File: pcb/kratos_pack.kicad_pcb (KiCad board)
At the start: 4 copper layers, 44.2 x 20.2 mm, 121 parts, among them J1 USB_C_Receptacle_USB2.0, J2 PROG_CONN, J3 DBG_UART, J4 BAT_MID+NTC, J5 BAT_7.4V, J6 BAT_0V, J7 OUT+, J8 OUT-, Q1 AON7403, Q2 AON7414, Q3 AON7414, Q4 UT6MA2TCR, Q5 UT6MA2TCR, Q6 UT6MA2TCR, SW1 WAKEUP, SW2 BOOT, SW3 RST_BTN, U1 USBLC6-2SC6, U10 24LC32, U11 MIC94300, U12 74LVC2G14, U13 MIC94300, U2 CP2102N-Axx-xQFN20, U3 STM32G071Gx, U4 KTD2026BEWE, U5 BQ25887, U6 BD48xxFVE, U7 INA199, U8 LTC4231, U9 LDK715M33R

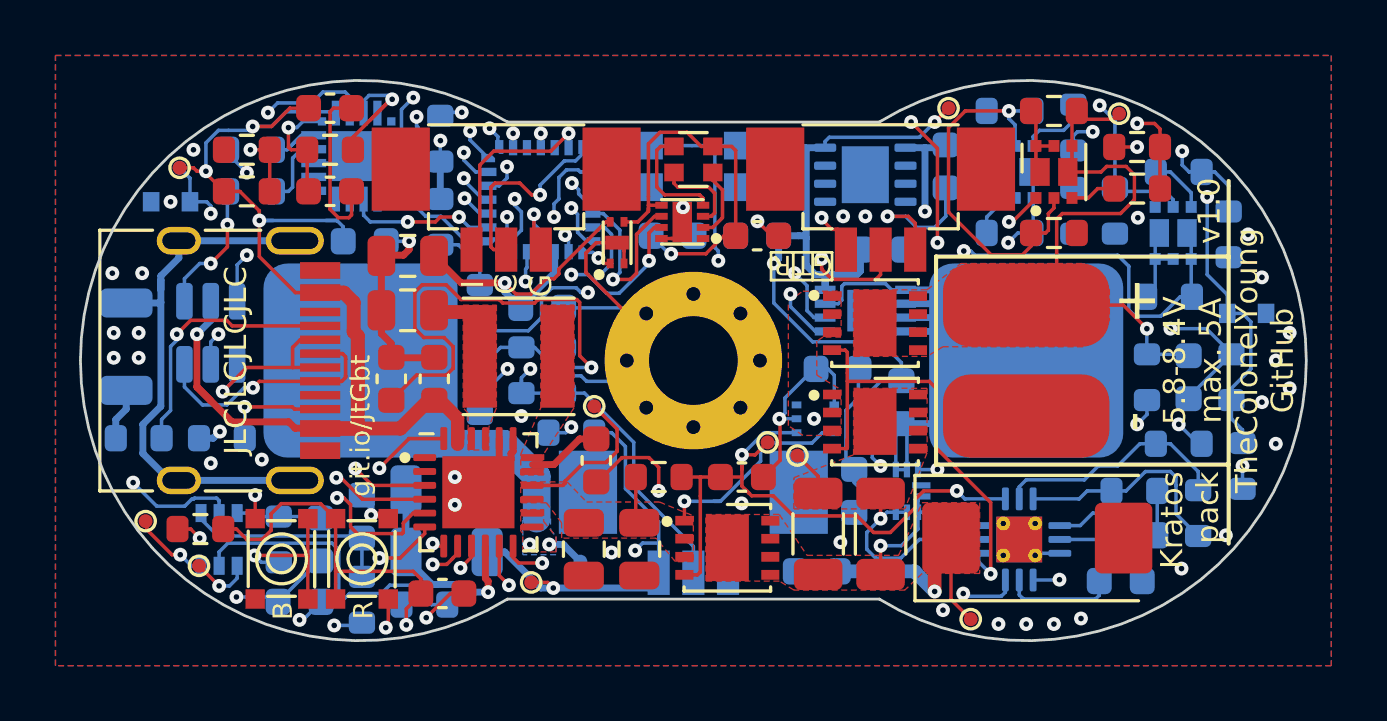
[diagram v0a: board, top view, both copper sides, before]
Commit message: Schema & PCB: add pull up to wakeup button
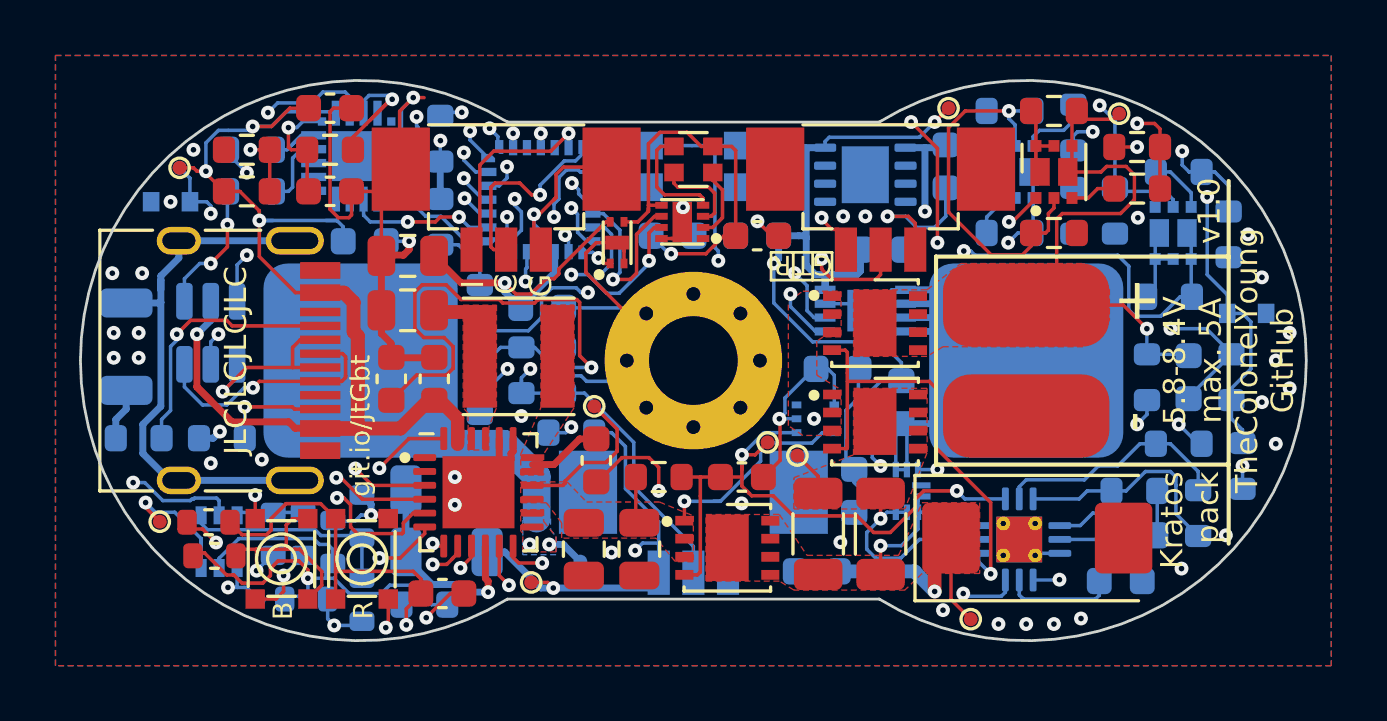
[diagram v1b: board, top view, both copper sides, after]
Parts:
- added R43: R, TCY_passives:R_0603_1608Metric, B.Cu at (137.0, 108.6)
- added R44: R, TCY_passives:R_0603_1608Metric, F.Cu at (133.7, 107.0)
- C1, C27, C28: footprint Capacitor_SMD:C_0603_1608Metric -> TCY_passives:C_0603_1608Metric
- R19, R35, R36: footprint Resistor_SMD:R_0603_1608Metric -> TCY_passives:R_0603_1608Metric
- TP14: moved to B.Cu
- moved TP14 2.48 mm to (135.3, 108.6), turned to 180 degrees
- moved C1 2.47 mm to (138.0, 106.5), turned to 90 degrees
- moved C28 0.65 mm to (136.9, 106.2)
- moved TP12 0.51 mm to (131.8, 105.8)
- moved R19 0.38 mm to (133.5, 105.8)
- moved R36 0.28 mm to (135.8, 106.2)
- moved U12 0.08 mm to (133.9, 106.5)
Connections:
- J2 pad ~: (no net) -> GND
- J3 pad ~: (no net) -> GND
- J4 pad ~: (no net) -> GND
- Q4 pad 3: /DIV_1 -> /DIV
- Q5 pad 3: /DIV_2 -> /DIV_1
- Q6 pad 3: /DIV -> /DIV_2
- R16 pad 1: /DIV -> /DIV_2
- R3 pad 1: /DIV_1 -> /DIV
- R8 pad 1: /DIV_2 -> /DIV_1
- U10 pad 9: (no net) -> GND
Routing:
- net GND: track 131.0 -> 149.0 mm
- net +3V3: track 84.0 -> 88.2 mm
- net /IN_1: track 5.81 -> 8.26 mm
- net /IN: track 30.1 -> 31.2 mm
- net /DIV_2: track 2.60 -> 1.68 mm
- net Net-(C28-Pad1): track 3.07 -> 2.42 mm
- net /BOOTL: track 24.4 -> 23.8 mm
- net /RESET: track 18.5 -> 19.1 mm
- net /DIV_1: track 2.10 -> 2.60 mm

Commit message: PCB: connector mounting point to ground, change LDk package to SOT-23-5
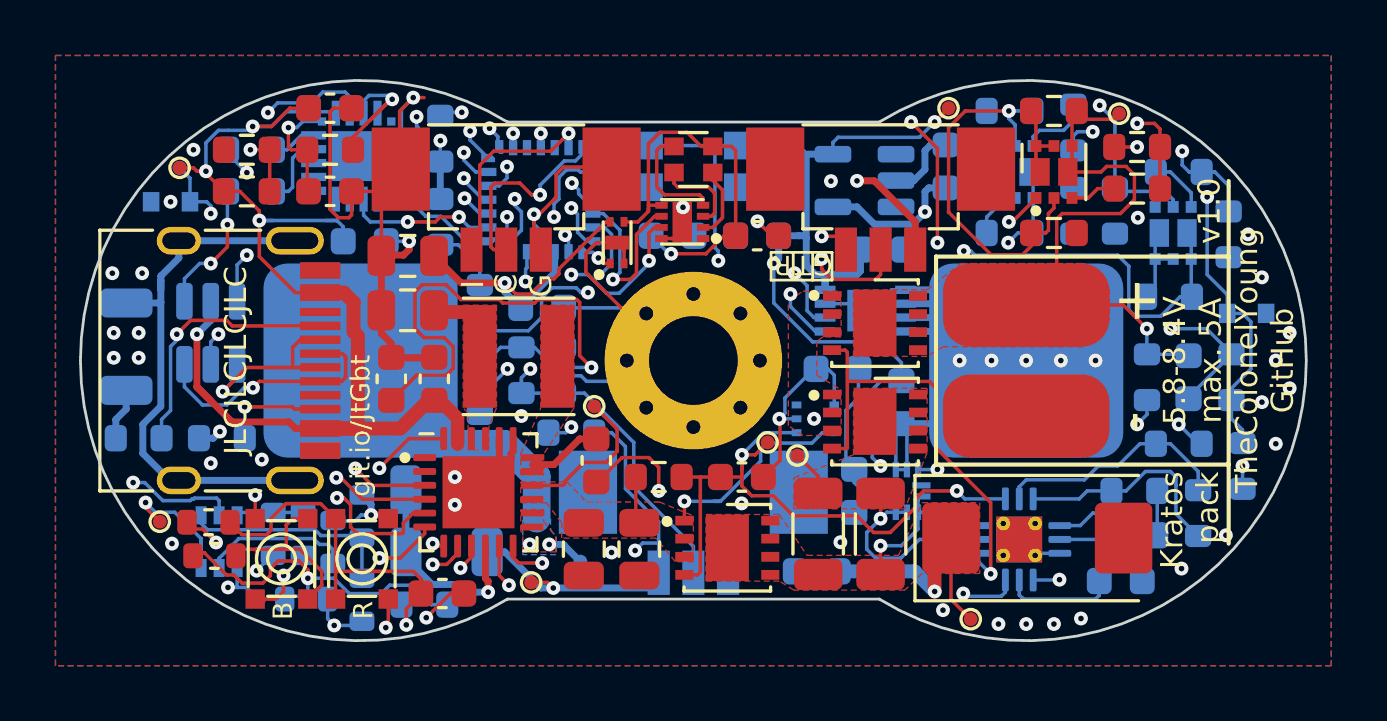
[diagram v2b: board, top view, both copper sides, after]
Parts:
- U9: footprint Package_DFN_QFN:DFN-8-1EP_3x3mm_P0.65mm_EP1.7x2.05mm -> Package_TO_SOT_SMD:SOT-23-5
- moved U9 0.21 mm to (157.2, 93.5)
- turned C22 to 90 degrees
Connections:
- R35 pad 2: /IN -> /IN_1
- R36 pad 2: /IN_1 -> /IN
- R43 pad 2: /IN -> /IN_1
- R44 pad 2: /IN_1 -> /IN
- SW1 pad 2: /IN -> /IN_1
- SW2 pad 2: /IN_1 -> /IN
- U9 pad 1: VCC -> (no net)
- U9 pad 2: (no net) -> GND
- U9 pad 4: GND -> VCC
- U9 pad 5: (no net) -> +3V3
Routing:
- net /IN_1: track 8.26 -> 31.2 mm, vias 1 -> 2
- net /IN: track 31.2 -> 8.26 mm, vias 2 -> 1
- net VCC: track 54.7 -> 56.2 mm
- net GND: track 149.0 -> 149.9 mm, vias 51 -> 56

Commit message: Schema & PCB: reconect output of charger from SNS to VBAT
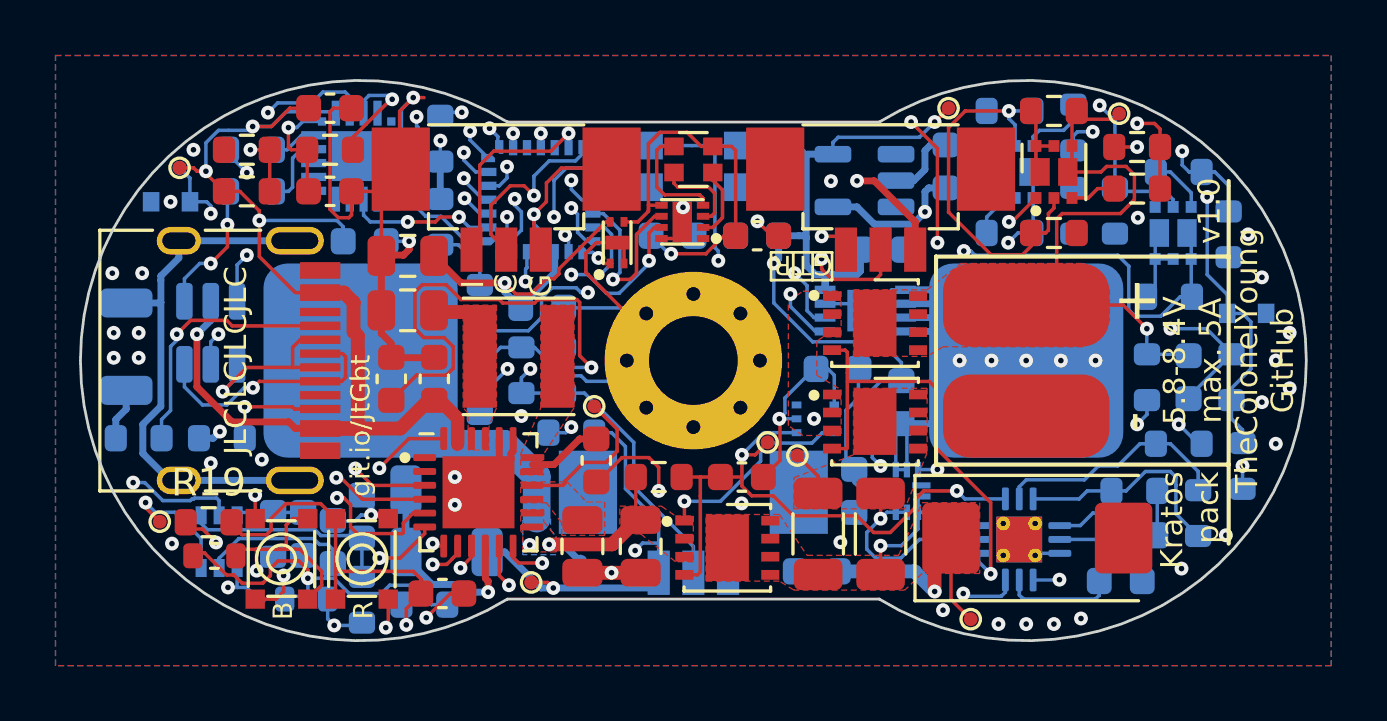
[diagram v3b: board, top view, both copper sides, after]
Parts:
- removed G*** (x2): LOGO, LOGO
- C1, C27, C28: footprint TCY_passives:C_0603_1608Metric -> Capacitor_SMD:C_0603_1608Metric
- C14: value 10uF -> 22uF
- R19, R35, R36: footprint TCY_passives:R_0603_1608Metric -> Resistor_SMD:R_0603_1608Metric
- R43, R44: value R -> 470k
- TP3: value B2_V -> VBAT
- TP4: value VBAT -> SNS
- moved C14 2.05 mm to (147.0, 106.7)
- moved C16 2.05 mm to (149.1, 106.7), turned to 90 degrees
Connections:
- net /DIV renamed /Voltage_measuring/DIV
- net /DIV_1 renamed /Voltage_measuring1/DIV
- net /DIV_2 renamed /Voltage_measuring2/DIV
- net /IN renamed /BTN_Denoise_BOOT/IN
- net /IN_1 renamed /BTN_Denoise_WAKE/IN
- C14 pad 1: /VBAT -> Net-(C14-Pad1)
- C16 pad 1: /VBAT -> GND
- C16 pad 2: GND -> /VBAT
- J1 pad A8: no_connect_78 -> unconnected-(J1-PadA8)
- J1 pad B8: no_connect_79 -> unconnected-(J1-PadB8)
- J5 pad 1: /B2_V -> /VBAT
- Q4 pad 4: /B2_V -> /VBAT
- Q4 pad 8: /B2_V -> /VBAT
- R34 pad 1: /B2_V -> /VBAT
- TP3 pad 1: /B2_V -> /VBAT
- TP4 pad 1: /VBAT -> Net-(C14-Pad1)
- U2 pad 1: no_connect_80 -> unconnected-(U2-Pad1)
- U2 pad 10: no_connect_95 -> unconnected-(U2-Pad10)
- U2 pad 11: no_connect_81 -> unconnected-(U2-Pad11)
- U2 pad 14: no_connect_82 -> unconnected-(U2-Pad14)
- U2 pad 15: no_connect_83 -> unconnected-(U2-Pad15)
- U2 pad 16: no_connect_84 -> unconnected-(U2-Pad16)
- U2 pad 19: no_connect_85 -> unconnected-(U2-Pad19)
- U2 pad 2: no_connect_86 -> unconnected-(U2-Pad2)
- U2 pad 20: no_connect_87 -> unconnected-(U2-Pad20)
- U3 pad 17: no_connect_88 -> unconnected-(U3-Pad17)
- U3 pad 19: no_connect_89 -> unconnected-(U3-Pad19)
- U3 pad 22: no_connect_90 -> unconnected-(U3-Pad22)
- U3 pad 24: no_connect_91 -> unconnected-(U3-Pad24)
- U4 pad 1: no_connect_92 -> unconnected-(U4-Pad1)
- U5 pad 1: no_connect_93 -> unconnected-(U5-Pad1)
- U5 pad 13: /B2_V -> /VBAT
- U5 pad 14: /B2_V -> /VBAT
- U5 pad 15: /VBAT -> Net-(C14-Pad1)
- U5 pad 16: /VBAT -> Net-(C14-Pad1)
- U5 pad 2: no_connect_94 -> unconnected-(U5-Pad2)
- U6 pad 3: (no net) -> unconnected-(U6-Pad3)
- U7 pad 1: (no net) -> unconnected-(U7-Pad1)
- U7 pad 7: (no net) -> unconnected-(U7-Pad7)
- U9 pad 1: (no net) -> unconnected-(U9-Pad1)
- U9 pad 3: (no net) -> unconnected-(U9-Pad3)
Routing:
- net /B2_V: track 47.2 -> 0.00 mm, vias 3 -> 0
- net /VBAT: track 14.9 -> 60.2 mm, vias 1 -> 4
- net Net-(C14-Pad1): track 0.00 -> 5.58 mm
- net VBUS: track 53.9 -> 52.3 mm
- net GND: track 149.9 -> 151.0 mm
- net Net-(R7-Pad2): track 5.11 -> 4.05 mm
- net /ME_EN: track 43.1 -> 42.2 mm
- net /UVLO: track 22.5 -> 21.8 mm
- net /D-: track 2.17 -> 1.65 mm
- net /SWCLK: track 7.35 -> 6.84 mm
- added copper zone on B.Cu, net /VBAT
- added copper zone on F.Cu, net Net-(C14-Pad1)
- removed copper zone on B.Cu, net /B2_V
- removed copper zone on F.Cu, net /B2_V

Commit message: PCB: change footprint of resistors and capacitors to smaller version
After first version is apparent that smaller footprint used on some
resistors are big enough for manual soldering. Because of this was
exchanged for custom smaller version.

In current version pull-up resistor of reset circuit is not connected,
because is mend to be removed in future.
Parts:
- C1, C10, C11, C13, C18, C19, C20, C21, C22, C23, C24, C25, C26, C27, C28, C29, C3, C30, C4, C5, C6, C8, C9: footprint Capacitor_SMD:C_0603_1608Metric -> TCY_passives:C_0603_1608Metric
- C12, C14, C16, C7: footprint Capacitor_SMD:C_0805_2012Metric -> TCY_passives:C_0805_2012Metric
- R1, R10, R11, R12, R13, R14, R15, R16, R17, R18, R19, R2, R20, R21, R22, R25, R26, R27, R3, R30, R31, R32, R33, R34, R35, R36, R37, R38, R39, R4, R40, R41, R42, R5, R6, R7, R8, R9: footprint Resistor_SMD:R_0603_1608Metric -> TCY_passives:R_0603_1608Metric
- moved R43 4.31 mm to (141.3, 108.7), turned to 180 degrees
- moved R18 4.08 mm to (137.2, 108.6), turned to 0 degrees
- moved R35 0.84 mm to (139.6, 108.0)
- moved C27 0.55 mm to (139.6, 105.4)
- moved C1 0.45 mm to (138.3, 106.2)
- moved R23 0.35 mm to (142.4, 104.6)
- moved R24 0.35 mm to (142.4, 106.8)
- moved C28 0.18 mm to (137.1, 106.2)
- moved R19 0.10 mm to (133.6, 105.9)
- moved R36 0.07 mm to (135.9, 106.2)
- turned C10 to 180 degrees
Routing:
- net +3V3: track 88.3 -> 83.9 mm
- net /TS: track 21.4 -> 25.2 mm
- net /CH_INT: track 22.8 -> 25.1 mm
- net GND: track 151.0 -> 149.2 mm, vias 56 -> 55
- net /SCL: track 35.7 -> 34.4 mm
- net /BTN_Denoise_WAKE/IN: track 31.2 -> 31.9 mm
- net Net-(R23-Pad1): track 7.65 -> 7.07 mm

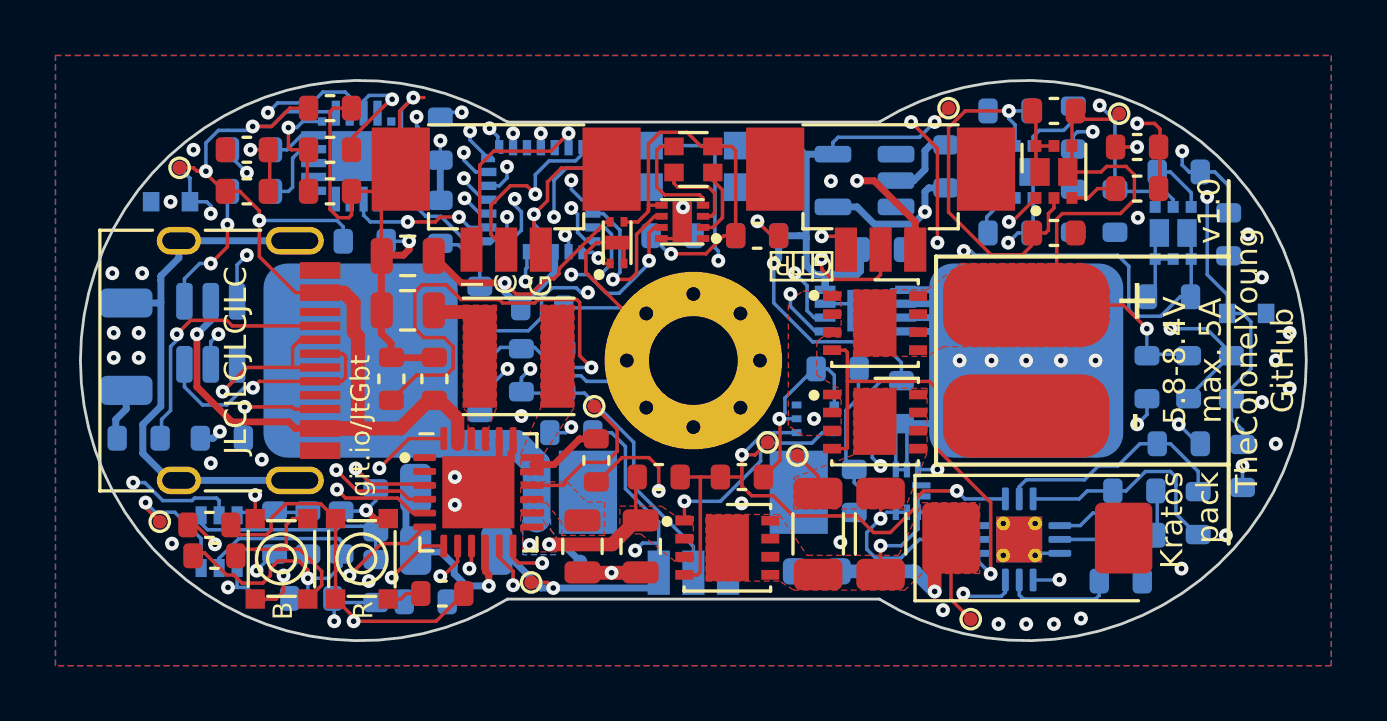
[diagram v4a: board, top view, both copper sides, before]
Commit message: Schema & PCB: Remove resistor in series with RESET line
Also some passive components around was shifter which resulted in better
clearance from edge of PCB.
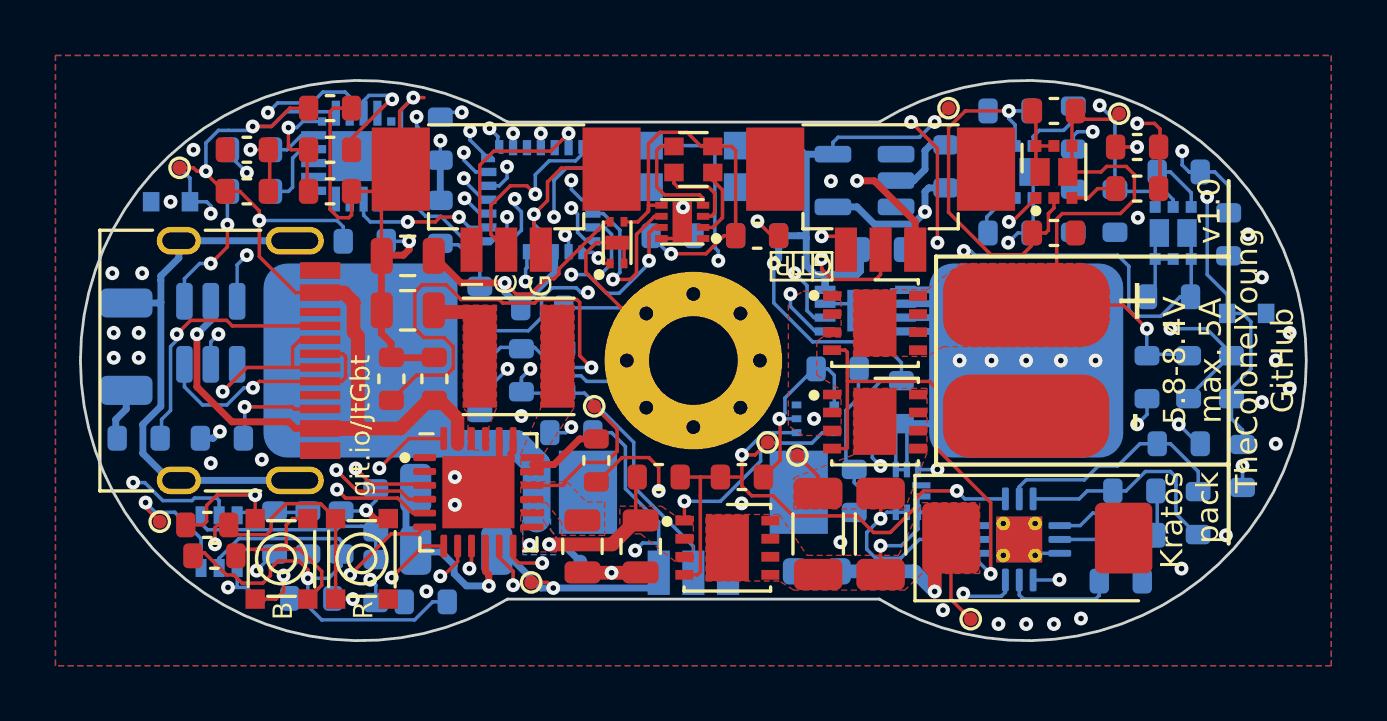
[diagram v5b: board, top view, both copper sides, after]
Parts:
- removed R19: 1k, TCY_passives:R_0603_1608Metric
- moved C10 8.83 mm to (133.5, 105.9)
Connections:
- C10 pad 1: Net-(C10-Pad1) -> /RESET
- R18 pad 2: Net-(C10-Pad1) -> /RESET
- SW3 pad 1: Net-(C10-Pad1) -> /RESET
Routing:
- net Net-(C10-Pad1): track 13.3 -> 0.00 mm, vias 1 -> 0
- net /RESET: track 18.9 -> 28.0 mm, vias 2 -> 3
- net +3V3: track 83.9 -> 89.9 mm
- net GND: track 149.2 -> 151.2 mm, vias 55 -> 54
- net /BTN_Denoise_WAKE/IN: track 31.9 -> 30.7 mm
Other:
- board text removed: "JLCJLCJLCJLC"

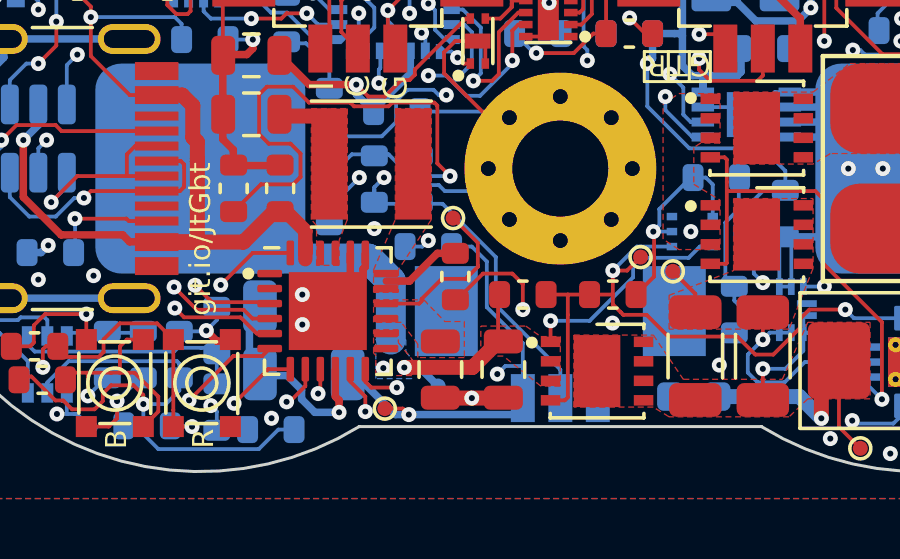
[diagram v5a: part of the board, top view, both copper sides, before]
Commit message: Schema & PCB: exchange SNS capacitor of charger IC for 47uF/16V in 1206
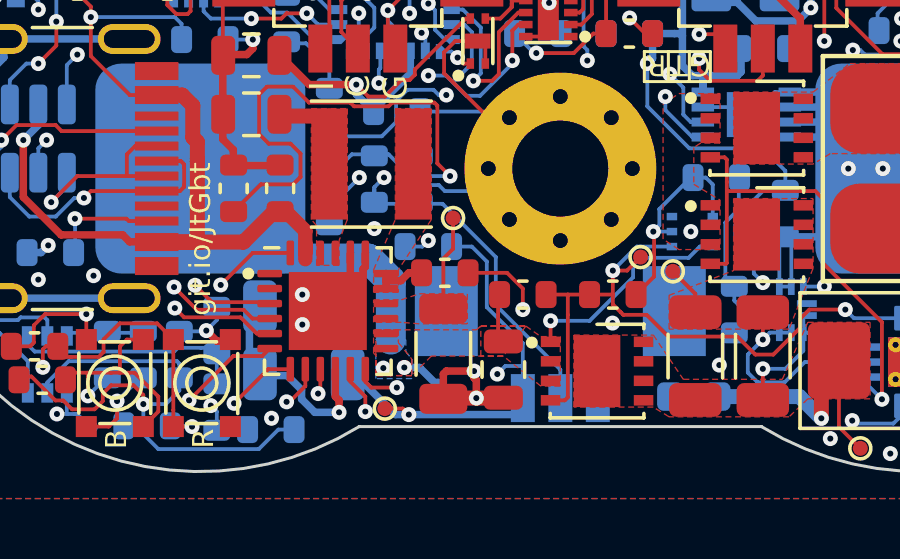
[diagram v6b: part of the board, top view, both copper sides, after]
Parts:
- C14: value 22uF -> 47uF/16V; footprint TCY_passives:C_0805_2012Metric -> TCY_passives:C_1206_3216Metric
- moved C14 0.53 mm to (147.1, 106.2)
- moved C9 0.37 mm to (147.2, 103.5), turned to 180 degrees
- turned C16 to -90 degrees
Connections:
- net Net-(C14-Pad1) renamed /SNS
- C16 pad 1: GND -> /VBAT
- C16 pad 2: /VBAT -> GND
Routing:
- net /VBAT: track 60.4 -> 56.6 mm
- net GND: track 151.2 -> 154.0 mm, vias 54 -> 55
- net /SNS: track 5.58 -> 3.16 mm
- net Net-(C9-Pad2): track 2.68 -> 1.80 mm
- net Net-(C9-Pad1): track 10.4 -> 9.56 mm
